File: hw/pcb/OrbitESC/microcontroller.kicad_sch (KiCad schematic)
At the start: 13 parts, among them J1 USB_C_Receptacle_USB2.0, J2 Micro_SD_Card_Det, J6 CAN1, J7 Serial1, U1 MCP2551-I-SN, U2 AT25SF081-SSHD-X, U3 24LC128, U4 STM32F446ZCHx

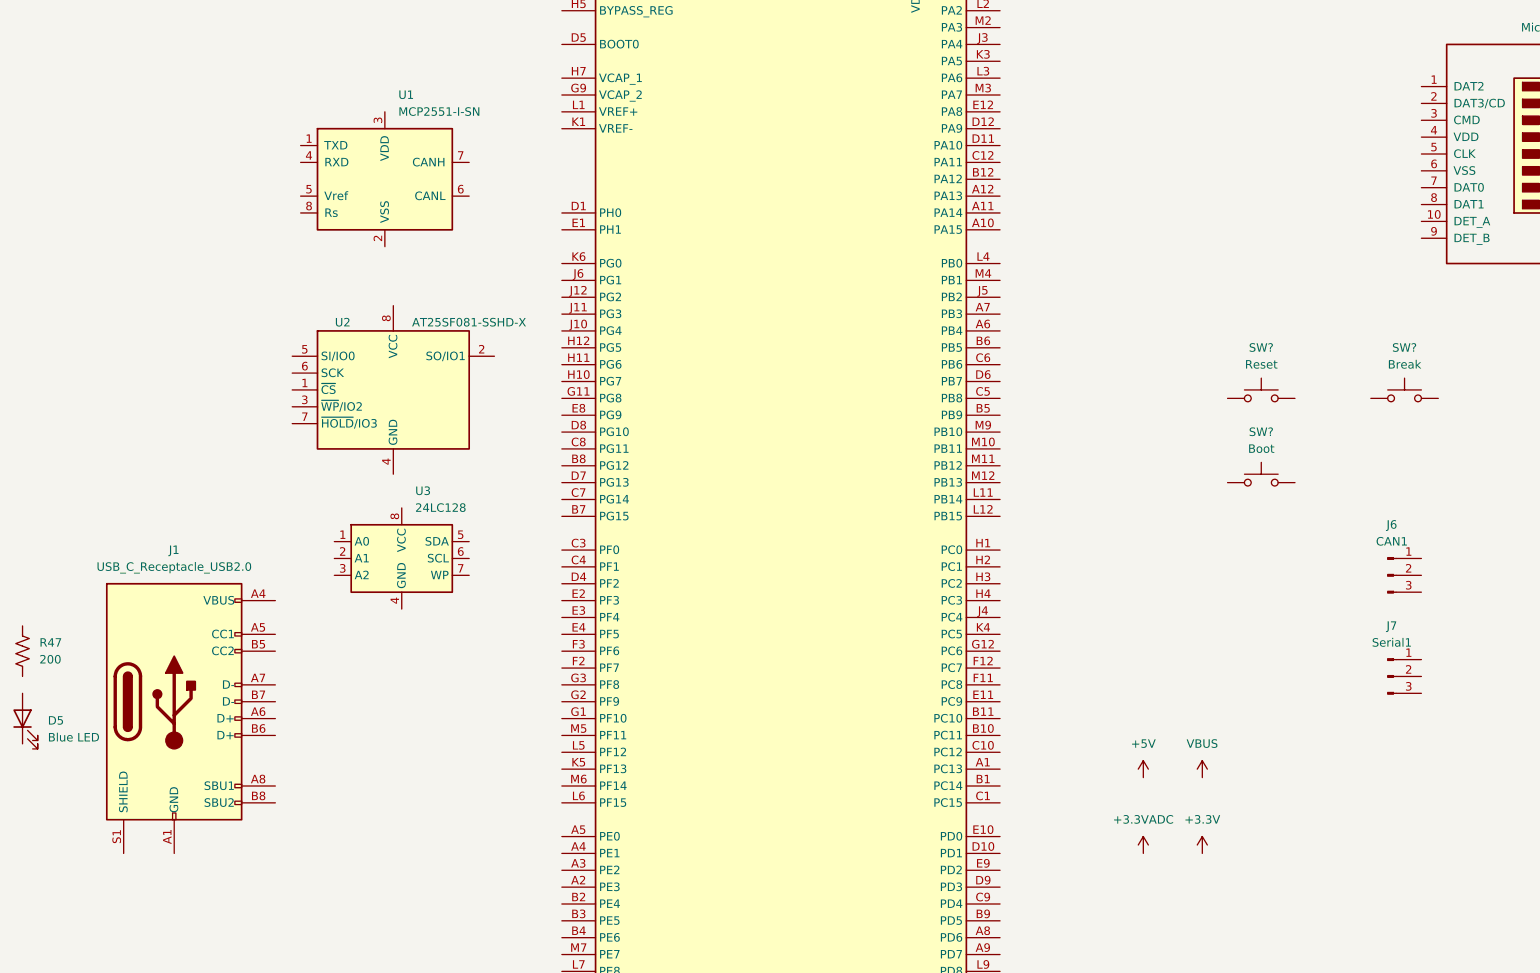
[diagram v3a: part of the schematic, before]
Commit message: Start working on USB interface
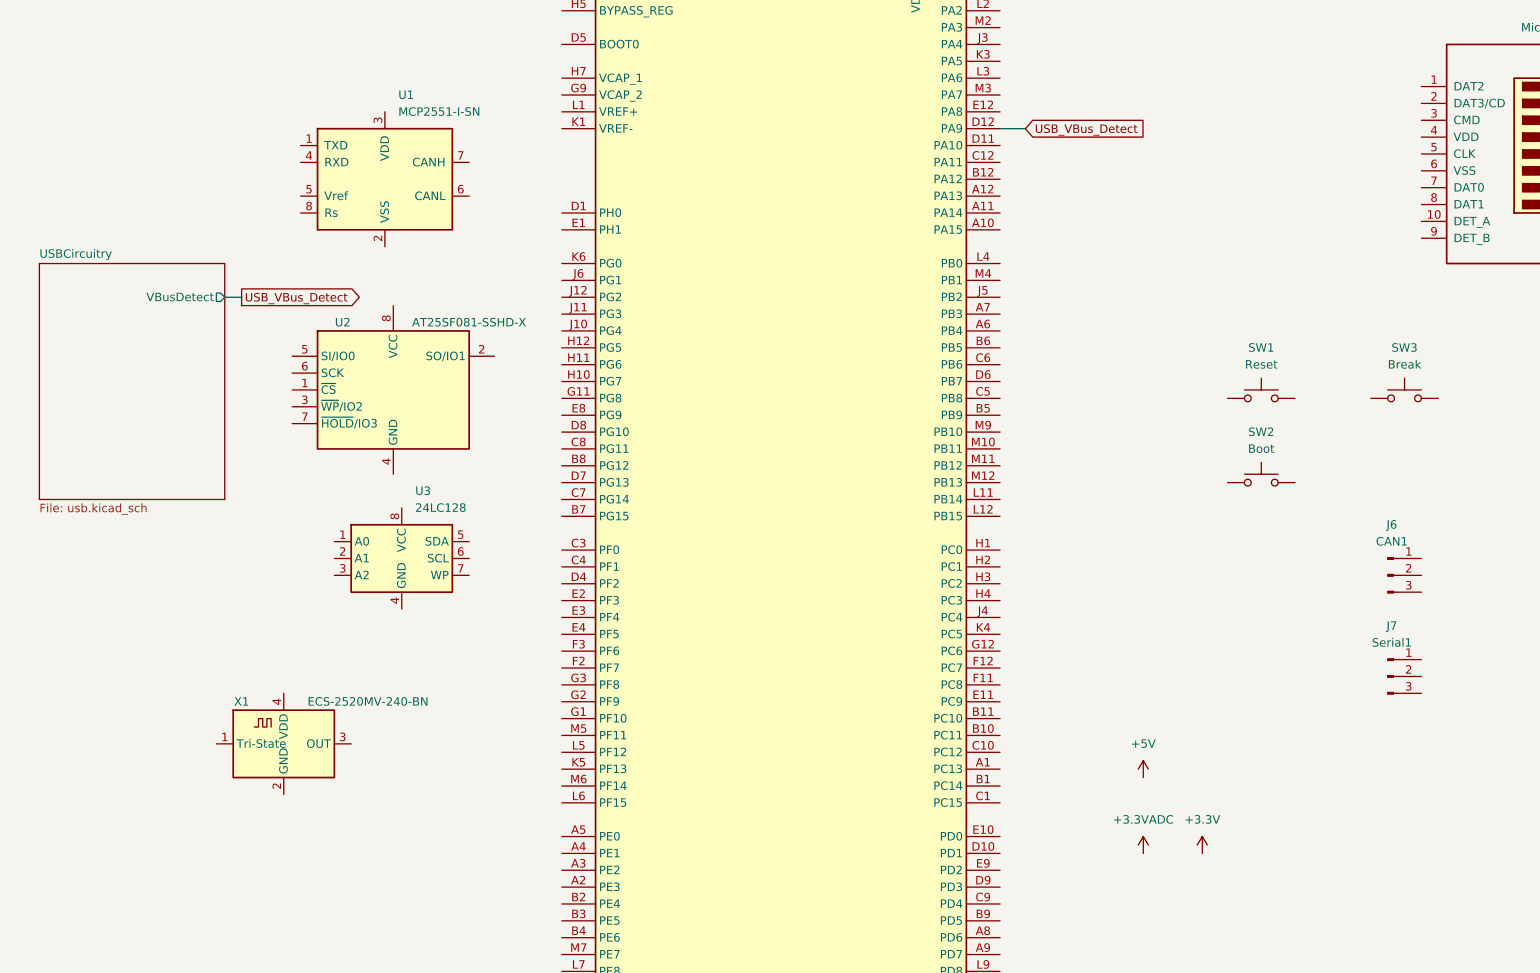
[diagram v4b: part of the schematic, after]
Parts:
- removed D5: Blue LED, Diode_SMD:D_0603_1608Metric, symbol Device:LED
- removed J1: USB_C_Receptacle_USB2.0, Connector_USB:USB_C_Receptacle_GCT_USB4085, symbol Connector:USB_C_Receptacle_USB2.0
- removed R47: 200, Resistor_SMD:R_0402_1005Metric, symbol Device:R_US
- added X1: ECS-2520MV-240-BN, Oscillator:Oscillator_SMD_ECS_2520MV-xxx-xx-4Pin_2.5x2.0mm, symbol Oscillator:ECS-2520MV-xxx-xx
- gave numbers to parts that had none: 3
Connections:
- net USB_VBus_Detect: now reaches U4.D12 (PA9)
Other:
- added sheet USBCircuitry (usb.kicad_sch)
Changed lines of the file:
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@@
 (kicad_sch (version 20211123) (generator eeschema)
   (paper "A4")
+  (wire (pts (xy 52.07 67.31) (xy 54.61 67.31))
+    (stroke (width 0) (type default) (color 0 0 0 0))
+  )
+  (wire (pts (xy 168.91 41.91) (xy 172.72 41.91))
+    (stroke (width 0) (type default) (color 0 0 0 0))
+  )
+  (global_label "USB_VBus_Detect" (shape output) (at 54.61 67.31 0) (fields_autoplaced)
+    (effects (font (size 1.27 1.27)) (justify left))
+    (property "Intersheet References" "${INTERSHEET_REFS}" (id 0) (at 73.2912 67.2306 0)
+      (effects (font (size 1.27 1.27)) (justify left) hide)
+    )
+  )
+  (global_label "USB_VBus_Detect" (shape input) (at 172.72 41.91 0) (fields_autoplaced)
+    (effects (font (size 1.27 1.27)) (justify left))
+    (property "Intersheet References" "${INTERSHEET_REFS}" (id 0) (at 191.4012 41.8306 0)
+      (effects (font (size 1.27 1.27)) (justify left) hide)
+    )
+  )
   (symbol (lib_id "power:+5V") (at 190.5 139.7 0) (unit 1)
     (in_bom yes) (on_board yes) (fields_autoplaced)
@@
   (symbol (lib_id "Switch:SW_Push") (at 229.87 82.55 0) (unit 1)
     (in_bom yes) (on_board yes) (fields_autoplaced)
-    (property "Reference" "SW?" (id 0) (at 229.87 74.93 0))
+    (property "Reference" "SW3" (id 0) (at 229.87 74.93 0))
     (property "Value" "Break" (id 1) (at 229.87 77.47 0))
     (property "Footprint" "Button_Switch_SMD:SW_SPST_PTS810" (id 2) (at 229.87 77.47 0)
@@
     (pin "1")
   )
-  (symbol (lib_id "Device:LED") (at 21.59 130.81 90) (unit 1)
-    (in_bom yes) (on_board yes) (fields_autoplaced)
-    (property "Reference" "D5" (id 0) (at 25.4 131.1274 90)
-      (effects (font (size 1.27 1.27)) (justify right))
-    )
-    (property "Value" "Blue LED" (id 1) (at 25.4 133.6674 90)
-      (effects (font (size 1.27 1.27)) (justify right))
-    )
-    (property "Footprint" "Diode_SMD:D_0603_1608Metric" (id 2) (at 21.59 130.81 0)
-      (effects (font (size 1.27 1.27)) hide)
-    )
-    (property "Datasheet" "https://datasheet.lcsc.com/lcsc/1811101510_Everlight-Elec-19-217-BHC-ZL1M2RY-3T_C72041.pdf" (id 3) (at 21.59 130.81 0)
-      (effects (font (size 1.27 1.27)) hide)
-    )
-    (property "JLCPCB" "C72041" (id 4) (at 21.59 130.81 90)
-      (effects (font (size 1.27 1.27)) hide)
-    )
-    (pin "1")
-    (pin "2")
+  (symbol (lib_id "Oscillator:ECS-2520MV-xxx-xx") (at 60.96 134.62 0) (unit 1)
+    (in_bom yes) (on_board yes)
+    (property "Reference" "X1" (id 0) (at 54.61 128.27 0))
+    (property "Value" "ECS-2520MV-240-BN" (id 1) (at 73.66 128.27 0))
+    (property "Footprint" "Oscillator:Oscillator_SMD_ECS_2520MV-xxx-xx-4Pin_2.5x2.0mm" (id 2) (at 72.39 143.51 0)
+      (effects (font (size 1.27 1.27)) hide)
+    )
+    (property "Datasheet" "https://www.ecsxtal.com/store/pdf/ECS-2520MV.pdf" (id 3) (at 56.515 131.445 0)
+      (effects (font (size 1.27 1.27)) hide)
+    )
+    (property "DigiKey" "XC2750CT-ND" (id 4) (at 60.96 134.62 0)
+      (effects (font (size 1.27 1.27)) hide)
+    )
+    (pin "1")
+    (pin "2")
+    (pin "3")
+    (pin "4")
   )
   (symbol (lib_id "Connector:Micro_SD_Card_Det") (at 255.27 45.72 0) (unit 1)
@@
     (pin "8")
     (pin "9")
-  )
-  (symbol (lib_id "Connector:USB_C_Receptacle_USB2.0") (at 44.45 128.27 0) (unit 1)
-    (in_bom yes) (on_board yes) (fields_autoplaced)
-    (property "Reference" "J1" (id 0) (at 44.45 105.41 0))
-    (property "Value" "USB_C_Receptacle_USB2.0" (id 1) (at 44.45 107.95 0))
-    (property "Footprint" "Connector_USB:USB_C_Receptacle_GCT_USB4085" (id 2) (at 48.26 128.27 0)
-      (effects (font (size 1.27 1.27)) hide)
-    )
-    (property "Datasheet" "https://www.usb.org/sites/default/files/documents/usb_type-c.zip" (id 3) (at 48.26 128.27 0)
-      (effects (font (size 1.27 1.27)) hide)
-    )
-    (property "DigiKey" "2073-USB4085-GF-ACT-ND" (id 4) (at 44.45 128.27 0)
-      (effects (font (size 1.27 1.27)) hide)
-    )
-    (pin "A1")
-    (pin "A12")
-    (pin "A4")
-    (pin "A5")
-    (pin "A6")
-    (pin "A7")
-    (pin "A8")
-    (pin "A9")
-    (pin "B1")
-    (pin "B12")
-    (pin "B4")
-    (pin "B5")
-    (pin "B6")
-    (pin "B7")
-    (pin "B8")
-    (pin "B9")
-    (pin "S1")
   )
   (symbol (lib_id "Interface_CAN_LIN:MCP2551-I-SN") (at 76.2 49.53 0) (unit 1)
@@
     (pin "8")
   )
-  (symbol (lib_id "power:VBUS") (at 199.39 139.7 0) (unit 1)
-    (in_bom yes) (on_board yes) (fields_autoplaced)
-    (property "Reference" "#PWR040" (id 0) (at 199.39 143.51 0)
-      (effects (font (size 1.27 1.27)) hide)
-    )
-    (property "Value" "VBUS" (id 1) (at 199.39 134.62 0))
-    (property "Footprint" "" (id 2) (at 199.39 139.7 0)
-      (effects (font (size 1.27 1.27)) hide)
-    )
-    (property "Datasheet" "" (id 3) (at 199.39 139.7 0)
-      (effects (font (size 1.27 1.27)) hide)
-    )
-    (pin "1")
-  )
   (symbol (lib_id "power:+3.3VADC") (at 190.5 151.13 0) (unit 1)
     (in_bom yes) (on_board yes) (fields_autoplaced)
@@
   (symbol (lib_id "Switch:SW_Push") (at 208.28 95.25 0) (unit 1)
     (in_bom yes) (on_board yes) (fields_autoplaced)
-    (property "Reference" "SW?" (id 0) (at 208.28 87.63 0))
+    (property "Reference" "SW2" (id 0) (at 208.28 87.63 0))
     (property "Value" "Boot" (id 1) (at 208.28 90.17 0))
     (property "Footprint" "Button_Switch_SMD:SW_SPST_PTS810" (id 2) (at 208.28 90.17 0)
@@
     )
     (property "Datasheet" "~" (id 3) (at 208.28 90.17 0)
-      (effects (font (size 1.27 1.27)) hide)
-    )
-    (pin "1")
-    (pin "2")
-  )
-  (symbol (lib_id "Device:R_US") (at 21.59 120.65 0) (unit 1)
-    (in_bom yes) (on_board yes) (fields_autoplaced)
-    (property "Reference" "R47" (id 0) (at 24.13 119.3799 0)
-      (effects (font (size 1.27 1.27)) (justify left))
-    )
-    (property "Value" "200" (id 1) (at 24.13 121.9199 0)
-      (effects (font (size 1.27 1.27)) (justify left))
-    )
-    (property "Footprint" "Resistor_SMD:R_0402_1005Metric" (id 2) (at 22.606 120.904 90)
-      (effects (font (size 1.27 1.27)) hide)
-    )
-    (property "Datasheet" "~" (id 3) (at 21.59 120.65 0)
-      (effects (font (size 1.27 1.27)) hide)
-    )
-    (property "JLCPCB" "C25087" (id 4) (at 21.59 120.65 0)
       (effects (font (size 1.27 1.27)) hide)
     )
@@
   (symbol (lib_id "Switch:SW_Push") (at 208.28 82.55 0) (unit 1)
     (in_bom yes) (on_board yes) (fields_autoplaced)
-    (property "Reference" "SW?" (id 0) (at 208.28 74.93 0))
+    (property "Reference" "SW1" (id 0) (at 208.28 74.93 0))
     (property "Value" "Reset" (id 1) (at 208.28 77.47 0))
     (property "Footprint" "Button_Switch_SMD:SW_SPST_PTS810" (id 2) (at 208.28 77.47 0)
@@
     (pin "2")
   )
+  (sheet (at 24.13 62.23) (size 27.94 35.56) (fields_autoplaced)
+    (stroke (width 0.1524) (type solid) (color 0 0 0 0))
+    (fill (color 0 0 0 0.0000))
+    (property "Sheet name" "USBCircuitry" (id 0) (at 24.13 61.5184 0)
+      (effects (font (size 1.27 1.27)) (justify left bottom))
+    )
+    (property "Sheet file" "usb.kicad_sch" (id 1) (at 24.13 98.3746 0)
+      (effects (font (size 1.27 1.27)) (justify left top))
+    )
+    (pin "VBusDetect" output (at 52.07 67.31 0)
+      (effects (font (size 1.27 1.27)) (justify right))
+    )
+  )
 )

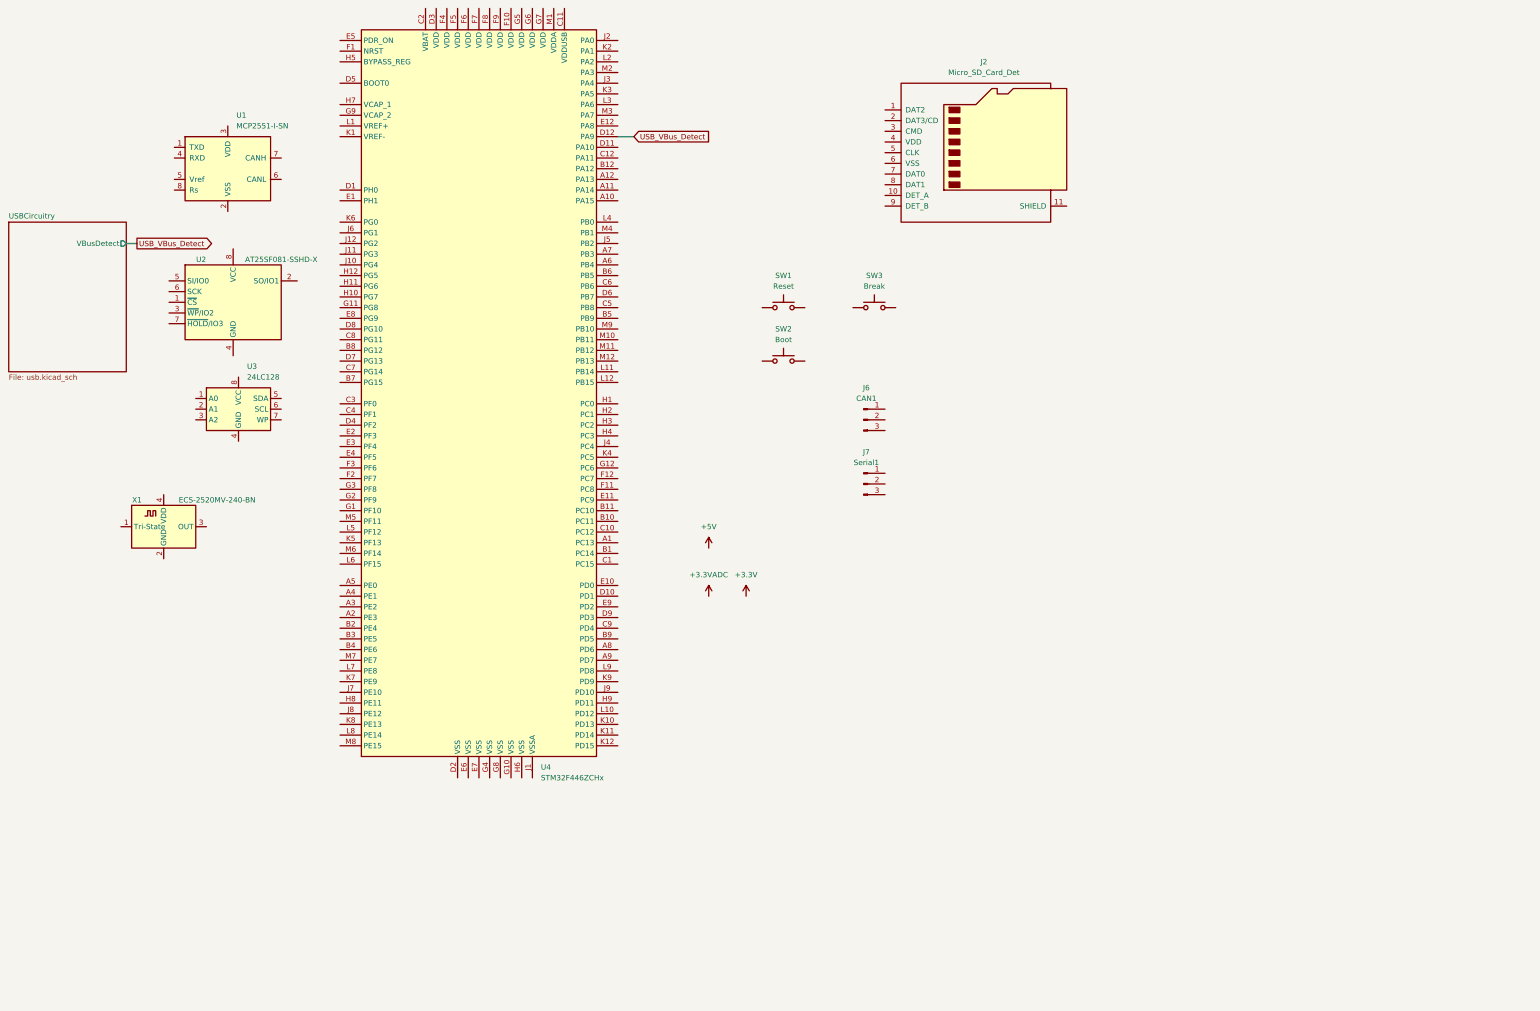
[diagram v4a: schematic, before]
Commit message: Connect USB to MCU
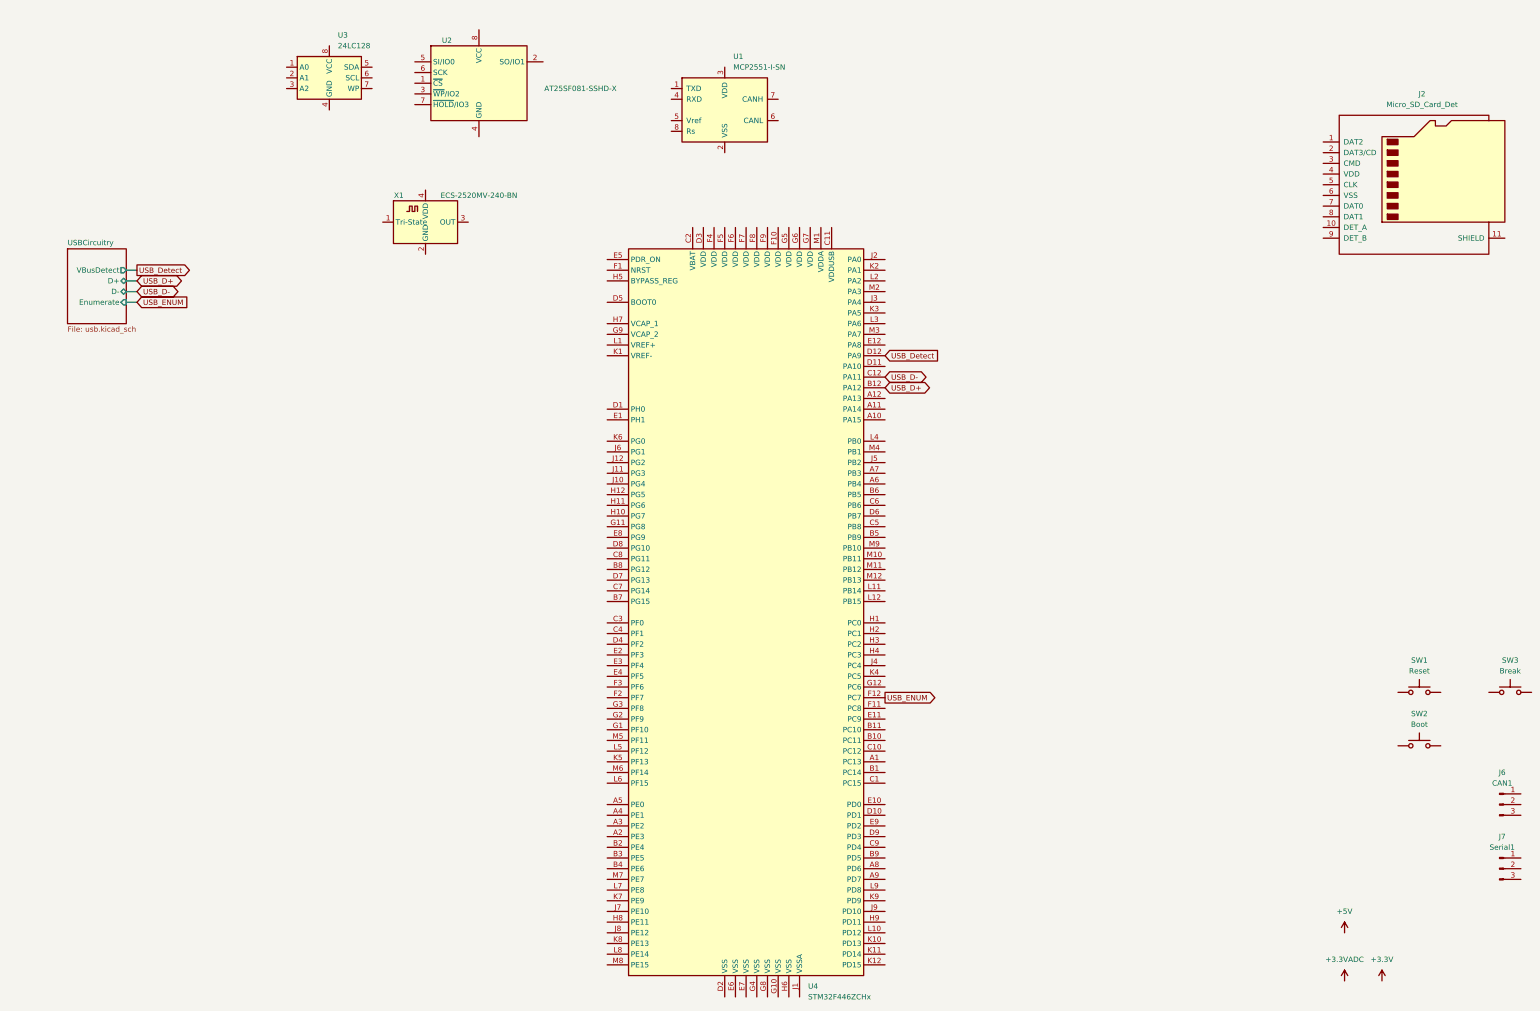
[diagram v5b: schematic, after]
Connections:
- net USB_D+: now reaches U4.B12 (PA12)
- net USB_D-: now reaches U4.C12 (PA11)
- net USB_ENUM: now reaches U4.F12 (PC7)
- net USB_VBus_Detect renamed USB_Detect
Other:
- sheet USBCircuitry ports: added D+, D-, Enumerate; removed none
- moved on the sheet: J2, J6, J7, SW1, SW2, SW3, U1, U2, U3, U4, X1
